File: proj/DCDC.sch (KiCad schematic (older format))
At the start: 26 parts, among them Q13 MMBT3904, Q14 MMBT2907A, Q15 MMBT3904

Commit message: Complete power supply design
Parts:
- removed C88, C?: 100u, symbol CPOL
- removed D3, D?: SCHOTTKY, symbol SCHOTTKY
- removed L6, L?: 220u, symbol LFERR
- removed Q14, Q?: MMBT2907A, IPC-semi-nominal:SOT-23, symbol MMBT2907A
- added C? (x4): 100u, IPC7351-Nominal:CAPAE660X570, symbol C-ALUM-660
- added C? (x5): 1u, IPC7351-Nominal:CAPC3216X70, symbol C-1206
- added C? (x2): 100n, IPC7351-Nominal:CAPC2012X70, symbol C-0805
- added C? (x2): 10u, IPC7351-Nominal:CAPC2012X70, symbol C-0805
- added C?: 22u, IPC7351-Nominal:CAPC2012X70, symbol C-0805
- added C? (x2): 1u, IPC7351-Nominal:CAPC2012X70, symbol C-0805
- added D? (x2): MBR0540, smd-semi:SOD-123, symbol MBR0540
- added D?: BAT54C, smd-semi:SOT-23, symbol BAT54C
- added L? (x2): 220u, manuf:BOURNS-RLB0914, symbol L-BOURNS-RLB0914
- added Q? (x2): PZT2907A, smd-semi:SOT-223, symbol PZT2907A
- added R?: THERM, symbol THERM
- added R? (x2): 2R2, IPC7351-Nominal:RESC1005X40, symbol R-0402
- added U?: L78M05CDT, smd-semi:TO-252, symbol L78MvvCDT
- added U?: MC79M05CDT, smd-semi:TO-252, symbol MC79MvvCDT
- added U?: AZ1117CH-1.8TRG1, smd-semi:SOT-223, symbol LM1117IMP-v.v
- added U?: MCP1700T-vv02E/TT, symbol MCP1700T-vv02E/TT
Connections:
- net labels added: FDBK_3V3, FDBK_N9, OUT+1V8, OUT+3V3MCU, OUT+5, OUT+9, OUT-5, SW_3V3, SW_N9, USB_IN
- wire segments 94 -> 114
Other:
- moved on the sheet: C?, DZ9, DZ?, Q?, R?

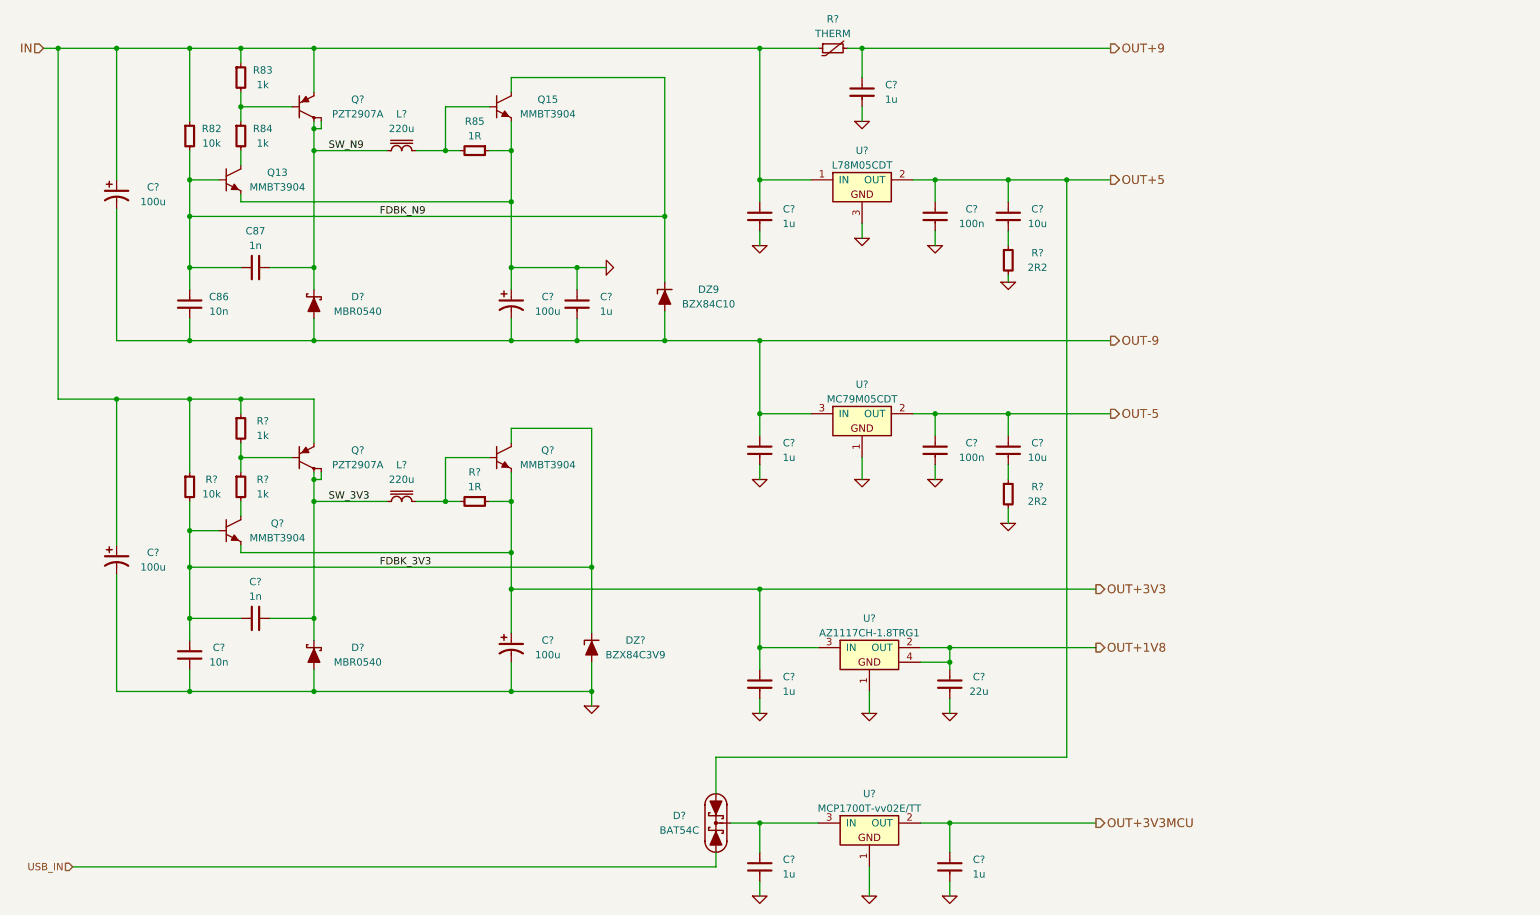
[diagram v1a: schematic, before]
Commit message: Finish USB subcircuit
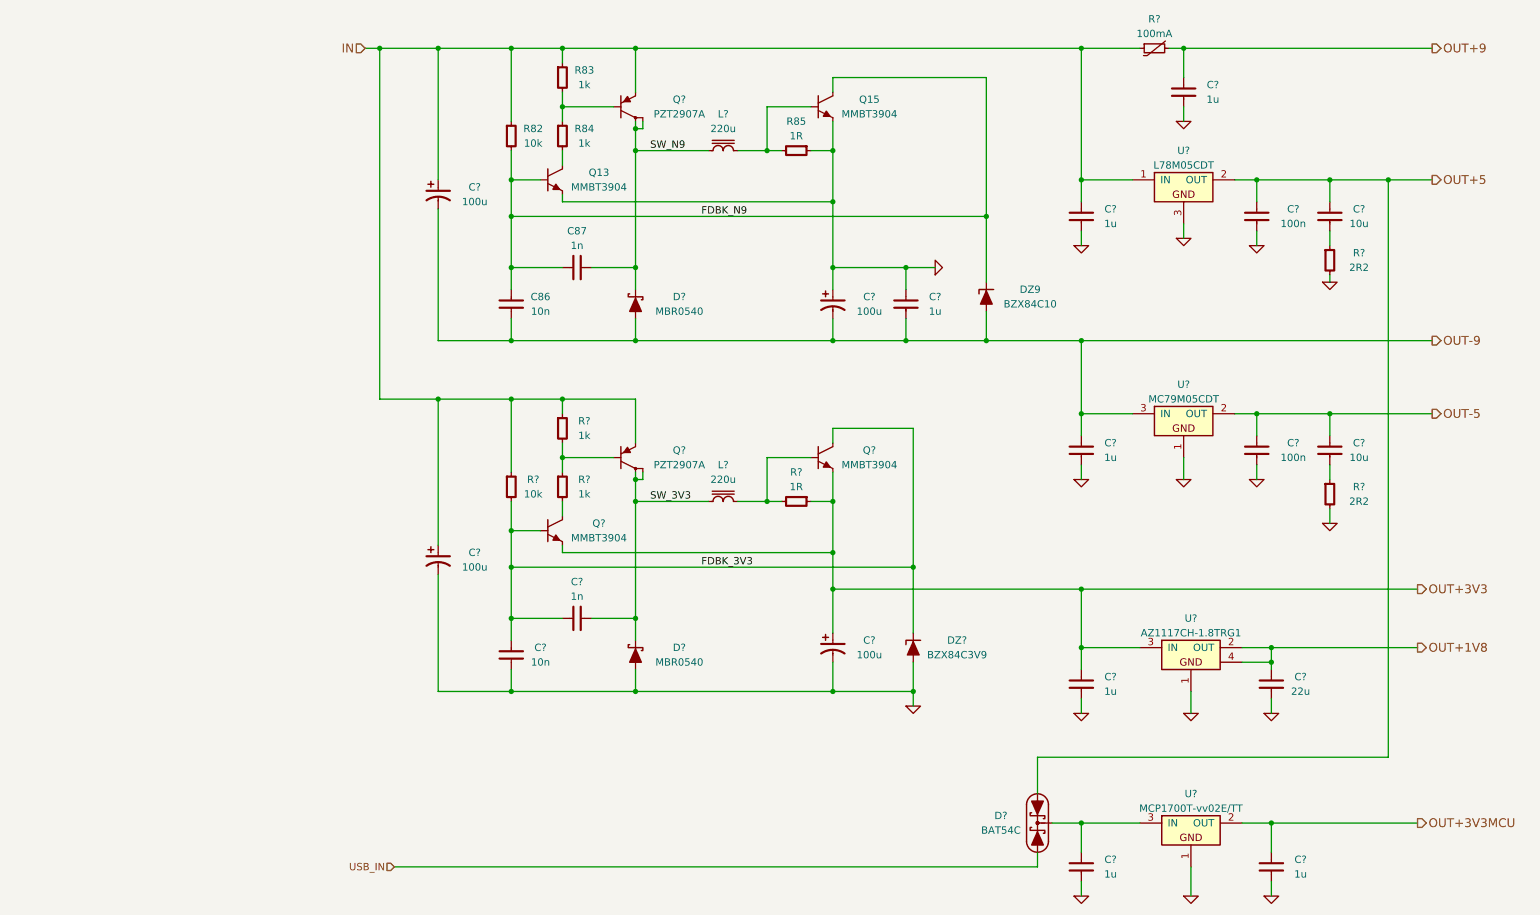
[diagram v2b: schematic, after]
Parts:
- removed R?: THERM, symbol THERM
- added R?: 100mA, IPC7351-Nominal:RESC3216X60, symbol THERM
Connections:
- net IN: now also R?.1
- net OUT+9: now also R?.2
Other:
- moved on the sheet: C86, C87, C?, D?, DZ9, DZ?, L?, Q13, Q15, Q?, R82, R83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

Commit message: Start PCB
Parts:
- U17: renamed from U?; footprint (none) -> smd-semi:SOT-23
- gave numbers to parts that had none: 38
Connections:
- net GND: now also C96.2
- net OUT-9: no longer C96.2

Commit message: Lots of routing
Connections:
- net ISEN_N9: now reaches L6.1, Q15.1, R85.2
- net ISEN_3V3: now reaches L7.1, Q19.1, R95.2
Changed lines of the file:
@@
 Wire Wire Line
 	4300 2900 10600 2900
+Text Label 6050 1300 0    50   ~ 0
+ISEN_N9
+Text Label 6050 3700 0    50   ~ 0
+ISEN_3V3
 $EndSCHEMATC

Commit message: Lots of layout work
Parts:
- added TP5: 3V3MCU, conn-test:TEST-SMD-SMALL, symbol TESTPOINT
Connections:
- net OUT+3V3MCU: now also TP5.1
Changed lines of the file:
@@
 P 7200 2400
 AR Path="/54F1FAAC/54F4F7B6/54F50066" Ref="#PWR8"  Part="1"
-AR Path="/54F4F7B6/54F50066" Ref="#PWR0245"  Part="1"
-F 0 "#PWR0245" H 7200 2400 30  0001 C CNN
+AR Path="/54F4F7B6/54F50066" Ref="#PWR0252"  Part="1"
+F 0 "#PWR0252" H 7200 2400 30  0001 C CNN
 F 1 "GND" H 7200 2330 30  0001 C CNN
 F 2 "" H 7200 2400 60  0000 C CNN
@@
 P 7050 5400
 AR Path="/54F1FAAC/54F4F7B6/54F543B2" Ref="#PWR?"  Part="1"
-AR Path="/54F4F7B6/54F543B2" Ref="#PWR0246"  Part="1"
-F 0 "#PWR0246" H 7050 5400 30  0001 C CNN
+AR Path="/54F4F7B6/54F543B2" Ref="#PWR0253"  Part="1"
+F 0 "#PWR0253" H 7050 5400 30  0001 C CNN
 F 1 "GND" H 7050 5330 30  0001 C CNN
 F 2 "" H 7050 5400 60  0000 C CNN
@@
 P 8900 1400
 AR Path="/54F1FAAC/54F4F7B6/54F64B84" Ref="#PWR?"  Part="1"
-AR Path="/54F4F7B6/54F64B84" Ref="#PWR0247"  Part="1"
-F 0 "#PWR0247" H 8900 1400 30  0001 C CNN
+AR Path="/54F4F7B6/54F64B84" Ref="#PWR0254"  Part="1"
+F 0 "#PWR0254" H 8900 1400 30  0001 C CNN
 F 1 "GND" H 8900 1330 30  0001 C CNN
 F 2 "" H 8900 1400 60  0000 C CNN
@@
 P 8900 2200
 AR Path="/54F1FAAC/54F4F7B6/54F676AE" Ref="#PWR?"  Part="1"
-AR Path="/54F4F7B6/54F676AE" Ref="#PWR0248"  Part="1"
-F 0 "#PWR0248" H 8900 2200 30  0001 C CNN
+AR Path="/54F4F7B6/54F676AE" Ref="#PWR0255"  Part="1"
+F 0 "#PWR0255" H 8900 2200 30  0001 C CNN
 F 1 "GND" H 8900 2130 30  0001 C CNN
 F 2 "" H 8900 2200 60  0000 C CNN
@@
 P 8200 2250
 AR Path="/54F1FAAC/54F4F7B6/54F67A48" Ref="#PWR?"  Part="1"
-AR Path="/54F4F7B6/54F67A48" Ref="#PWR0249"  Part="1"
-F 0 "#PWR0249" H 8200 2250 30  0001 C CNN
+AR Path="/54F4F7B6/54F67A48" Ref="#PWR0256"  Part="1"
+F 0 "#PWR0256" H 8200 2250 30  0001 C CNN
 F 1 "GND" H 8200 2180 30  0001 C CNN
 F 2 "" H 8200 2250 60  0000 C CNN
@@
 P 9400 2250
 AR Path="/54F1FAAC/54F4F7B6/54F687DB" Ref="#PWR?"  Part="1"
-AR Path="/54F4F7B6/54F687DB" Ref="#PWR0250"  Part="1"
-F 0 "#PWR0250" H 9400 2250 30  0001 C CNN
+AR Path="/54F4F7B6/54F687DB" Ref="#PWR0257"  Part="1"
+F 0 "#PWR0257" H 9400 2250 30  0001 C CNN
 F 1 "GND" H 9400 2180 30  0001 C CNN
 F 2 "" H 9400 2250 60  0000 C CNN
@@
 P 9900 2500
 AR Path="/54F1FAAC/54F4F7B6/54F6971F" Ref="#PWR?"  Part="1"
-AR Path="/54F4F7B6/54F6971F" Ref="#PWR0251"  Part="1"
-F 0 "#PWR0251" H 9900 2500 30  0001 C CNN
+AR Path="/54F4F7B6/54F6971F" Ref="#PWR0258"  Part="1"
+F 0 "#PWR0258" H 9900 2500 30  0001 C CNN
 F 1 "GND" H 9900 2430 30  0001 C CNN
 F 2 "" H 9900 2500 60  0000 C CNN
@@
 P 8200 3850
 AR Path="/54F1FAAC/54F4F7B6/54F6B841" Ref="#PWR?"  Part="1"
-AR Path="/54F4F7B6/54F6B841" Ref="#PWR0252"  Part="1"
-F 0 "#PWR0252" H 8200 3850 30  0001 C CNN
+AR Path="/54F4F7B6/54F6B841" Ref="#PWR0259"  Part="1"
+F 0 "#PWR0259" H 8200 3850 30  0001 C CNN
 F 1 "GND" H 8200 3780 30  0001 C CNN
 F 2 "" H 8200 3850 60  0000 C CNN
@@
 P 9900 4150
 AR Path="/54F1FAAC/54F4F7B6/54F6BEED" Ref="#PWR?"  Part="1"
-AR Path="/54F4F7B6/54F6BEED" Ref="#PWR0253"  Part="1"
-F 0 "#PWR0253" H 9900 4150 30  0001 C CNN
+AR Path="/54F4F7B6/54F6BEED" Ref="#PWR0260"  Part="1"
+F 0 "#PWR0260" H 9900 4150 30  0001 C CNN
 F 1 "GND" H 9900 4080 30  0001 C CNN
 F 2 "" H 9900 4150 60  0000 C CNN
@@
 P 9400 3850
 AR Path="/54F1FAAC/54F4F7B6/54F6BFFB" Ref="#PWR?"  Part="1"
-AR Path="/54F4F7B6/54F6BFFB" Ref="#PWR0254"  Part="1"
-F 0 "#PWR0254" H 9400 3850 30  0001 C CNN
+AR Path="/54F4F7B6/54F6BFFB" Ref="#PWR0261"  Part="1"
+F 0 "#PWR0261" H 9400 3850 30  0001 C CNN
 F 1 "GND" H 9400 3780 30  0001 C CNN
 F 2 "" H 9400 3850 60  0000 C CNN
@@
 P 8900 3850
 AR Path="/54F1FAAC/54F4F7B6/54F6C162" Ref="#PWR?"  Part="1"
-AR Path="/54F4F7B6/54F6C162" Ref="#PWR0255"  Part="1"
-F 0 "#PWR0255" H 8900 3850 30  0001 C CNN
+AR Path="/54F4F7B6/54F6C162" Ref="#PWR0262"  Part="1"
+F 0 "#PWR0262" H 8900 3850 30  0001 C CNN
 F 1 "GND" H 8900 3780 30  0001 C CNN
 F 2 "" H 8900 3850 60  0000 C CNN
@@
 P 8200 5450
 AR Path="/54F1FAAC/54F4F7B6/54F708B6" Ref="#PWR?"  Part="1"
-AR Path="/54F4F7B6/54F708B6" Ref="#PWR0256"  Part="1"
-F 0 "#PWR0256" H 8200 5450 30  0001 C CNN
+AR Path="/54F4F7B6/54F708B6" Ref="#PWR0263"  Part="1"
+F 0 "#PWR0263" H 8200 5450 30  0001 C CNN
 F 1 "GND" H 8200 5380 30  0001 C CNN
 F 2 "" H 8200 5450 60  0000 C CNN
@@
 P 8950 5450
 AR Path="/54F1FAAC/54F4F7B6/54F70A31" Ref="#PWR?"  Part="1"
-AR Path="/54F4F7B6/54F70A31" Ref="#PWR0257"  Part="1"
-F 0 "#PWR0257" H 8950 5450 30  0001 C CNN
+AR Path="/54F4F7B6/54F70A31" Ref="#PWR0264"  Part="1"
+F 0 "#PWR0264" H 8950 5450 30  0001 C CNN
 F 1 "GND" H 8950 5380 30  0001 C CNN
 F 2 "" H 8950 5450 60  0000 C CNN
@@
 P 9500 5450
 AR Path="/54F1FAAC/54F4F7B6/54F71350" Ref="#PWR?"  Part="1"
-AR Path="/54F4F7B6/54F71350" Ref="#PWR0258"  Part="1"
-F 0 "#PWR0258" H 9500 5450 30  0001 C CNN
+AR Path="/54F4F7B6/54F71350" Ref="#PWR0265"  Part="1"
+F 0 "#PWR0265" H 9500 5450 30  0001 C CNN
 F 1 "GND" H 9500 5380 30  0001 C CNN
 F 2 "" H 9500 5450 60  0000 C CNN
@@
 P 8200 6700
 AR Path="/54F1FAAC/54F4F7B6/54F777AE" Ref="#PWR?"  Part="1"
-AR Path="/54F4F7B6/54F777AE" Ref="#PWR0259"  Part="1"
-F 0 "#PWR0259" H 8200 6700 30  0001 C CNN
+AR Path="/54F4F7B6/54F777AE" Ref="#PWR0266"  Part="1"
+F 0 "#PWR0266" H 8200 6700 30  0001 C CNN
 F 1 "GND" H 8200 6630 30  0001 C CNN
 F 2 "" H 8200 6700 60  0000 C CNN
@@
 P 8950 6700
 AR Path="/54F1FAAC/54F4F7B6/54F779B8" Ref="#PWR?"  Part="1"
-AR Path="/54F4F7B6/54F779B8" Ref="#PWR0260"  Part="1"
-F 0 "#PWR0260" H 8950 6700 30  0001 C CNN
+AR Path="/54F4F7B6/54F779B8" Ref="#PWR0267"  Part="1"
+F 0 "#PWR0267" H 8950 6700 30  0001 C CNN
 F 1 "GND" H 8950 6630 30  0001 C CNN
 F 2 "" H 8950 6700 60  0000 C CNN
@@
 P 9500 6700
 AR Path="/54F1FAAC/54F4F7B6/54F78198" Ref="#PWR?"  Part="1"
-AR Path="/54F4F7B6/54F78198" Ref="#PWR0261"  Part="1"
-F 0 "#PWR0261" H 9500 6700 30  0001 C CNN
+AR Path="/54F4F7B6/54F78198" Ref="#PWR0268"  Part="1"
+F 0 "#PWR0268" H 9500 6700 30  0001 C CNN
 F 1 "GND" H 9500 6630 30  0001 C CNN
 F 2 "" H 9500 6700 60  0000 C CNN
@@
 $EndComp
 $Comp
-L GND #PWR0262
+L GND #PWR0269
 U 1 1 54F66084
 P 3800 2150
-F 0 "#PWR0262" H 3800 2150 30  0001 C CNN
+F 0 "#PWR0269" H 3800 2150 30  0001 C CNN
 F 1 "GND" H 3800 2080 30  0001 C CNN
 F 2 "" H 3800 2150 60  0000 C CNN
@@
 Text Label 6050 3700 0    50   ~ 0
 ISEN_3V3
+$Comp
+L TESTPOINT TP5
+U 1 1 54F863A1
+P 10150 6100
+F 0 "TP5" H 10350 6250 50  0000 C CNN
+F 1 "3V3MCU" H 10350 6150 50  0000 C CNN
+F 2 "conn-test:TEST-SMD-SMALL" H 10150 6100 50  0001 C CNN
+F 3 "" H 10150 6100 50  0000 C CNN
+	1    10150 6100
+	1    0    0    -1
+$EndComp
+Wire Wire Line
+	10150 6100 10150 6200
+Connection ~ 10150 6200
 $EndSCHEMATC
